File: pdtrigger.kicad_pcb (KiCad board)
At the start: 4 copper layers, 56 x 53 mm, 72 parts, among them J1 Conn_01x04_Pin, J2 USB_C_Receptacle_USB2.0_16P, Q1 DMP3098LSD-13, Q3 NMOS, SW1 SW_SPDT, U1 STM32F401RBT6, U2 CYPD3177-24LQXQ, U3 TERM_BLK, U4 SY8303AIC, Y1 16MHz

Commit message: Cleaned up schem
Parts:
- added C26: 1u, Capacitor_SMD:C_0402_1005Metric, F.Cu at (163.0, 114.5)
- added D3: YEL, LED_SMD:LED_0805_2012Metric, F.Cu at (165.2, 117.8)
- added D4: YEL, LED_SMD:LED_0805_2012Metric, F.Cu at (165.2, 120.5)
- added D5: YEL, LED_SMD:LED_0805_2012Metric, F.Cu at (165.2, 123.2)
- added D6: YEL, LED_SMD:LED_0805_2012Metric, F.Cu at (165.2, 126.0)
- added D7: YEL, LED_SMD:LED_0805_2012Metric, F.Cu at (165.2, 128.8)
- added G***: LOGO, dKiCadLib:dcLogo, F.Cu at (151.0, 137.0)
- added G***: LOGO, LOGO, F.Cu at (171.5, 112.8)
- added J3: Conn_01x02_Pin, libs:HDR-TH_2P-P2.54-V-M, F.Cu at (132.0, 97.0)
- added R27: 20k, Resistor_SMD:R_0603_1608Metric, F.Cu at (162.8, 111.9)
- added R28: 1k5, Resistor_SMD:R_0402_1005Metric, F.Cu at (163.0, 117.7)
- added R29: 1k5, Resistor_SMD:R_0402_1005Metric, F.Cu at (163.0, 120.5)
- added R30: 1k5, Resistor_SMD:R_0402_1005Metric, F.Cu at (163.0, 123.3)
- added R31: 1k5, Resistor_SMD:R_0402_1005Metric, F.Cu at (163.0, 126.0)
- added R32: 1k5, Resistor_SMD:R_0402_1005Metric, F.Cu at (163.0, 128.8)
- added SW2: SW_Push, libs:SW-SMD_L3.9-W3.0-P4.45, F.Cu at (166.5, 112.8)
- added TP1: TestPoint, TestPoint:TestPoint_THTPad_D1.5mm_Drill0.7mm, F.Cu at (180.0, 135.2)
- added TP2: TestPoint, TestPoint:TestPoint_THTPad_D1.5mm_Drill0.7mm, F.Cu at (175.0, 140.5)
- added TP3: TestPoint, TestPoint:TestPoint_THTPad_D1.5mm_Drill0.7mm, F.Cu at (134.0, 140.5)
- moved R13 0.75 mm to (143.2, 116.0)
- moved R18 0.50 mm to (151.8, 116.0)
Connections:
- net Net-(U4-LX) renamed /LX
- J2 pad S1: unconnected-(J2-SHIELD-PadS1)_2 -> GND
- U1 pad 16: unconnected-(U1-PA2-Pad16) -> /UART_TX
- U1 pad 17: unconnected-(U1-PA3-Pad17) -> /UART_RX
- U1 pad 54: unconnected-(U1-PD2-Pad54) -> /LED_PDO5
- U1 pad 55: unconnected-(U1-PB3-Pad55) -> /LED_PDO4
- U1 pad 56: unconnected-(U1-PB4-Pad56) -> /LED_PDO3
- U1 pad 57: unconnected-(U1-PB5-Pad57) -> /LED_PDO2
- U1 pad 58: unconnected-(U1-PB6-Pad58) -> /LED_PDO1
- U1 pad 59: unconnected-(U1-PB7-Pad59) -> /MODE_BTN
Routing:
- net Net-(C18-Pad2): track 10.6 -> 43.1 mm, vias 0 -> 2
- net /PD_FAULT: track 3.31 -> 31.6 mm, vias 0 -> 3
- net /LED_PDO5: track 0.00 -> 27.2 mm
- net /USB_D+: track 0.00 -> 26.9 mm, vias 0 -> 2
- net /SWDIO: track 0.00 -> 26.6 mm, vias 0 -> 1
- net /USB_D-: track 0.00 -> 26.0 mm, vias 0 -> 2
- net /LED_PDO4: track 0.00 -> 25.0 mm
- net /LED_PDO3: track 0.00 -> 22.8 mm
- net /BOOT0: track 0.00 -> 22.0 mm, vias 0 -> 2
- net /LED_PDO2: track 0.00 -> 20.7 mm
- net /SWCLK: track 0.00 -> 20.2 mm, vias 0 -> 1
- net /PD_SAFE: track 0.00 -> 18.5 mm
- net /LED_PDO1: track 0.00 -> 18.5 mm
- net /MODE_BTN: track 0.00 -> 17.4 mm
- net /UART_TX: track 0.00 -> 17.4 mm, vias 0 -> 1
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- added copper zone on In2.Cu, net +3V3_MCU
- added copper zone on F.Cu, net /LX
- added copper zone on B.Cu, net GND
- added copper zone on F.Cu, net GND
- added copper zone on In1.Cu, net GND
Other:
- board text added: "12V"
- board text added: "15V"
- board text added: "20V"
- board text added: "5V"
- board text added: "9V"
- board text added: "GND"
- board text added: "JLCJLCJLCJLC"
- board text added: "LC 3 Sep 2025"
- board text added: "PDO"
- board text added: "RX"
- board text added: "TX"
- board text added: "USB-C PD Trigger"
- board text added: "VIN"
- board text added: "VOUT"
- board text removed: "DNP"

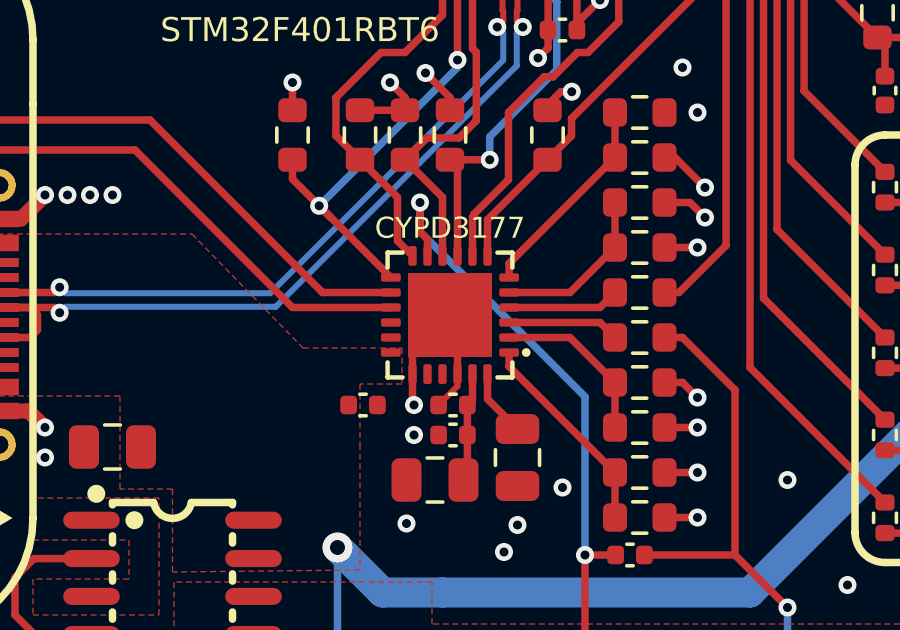
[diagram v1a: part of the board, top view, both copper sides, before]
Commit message: added GND via-in-pad to CYPD3177 IC
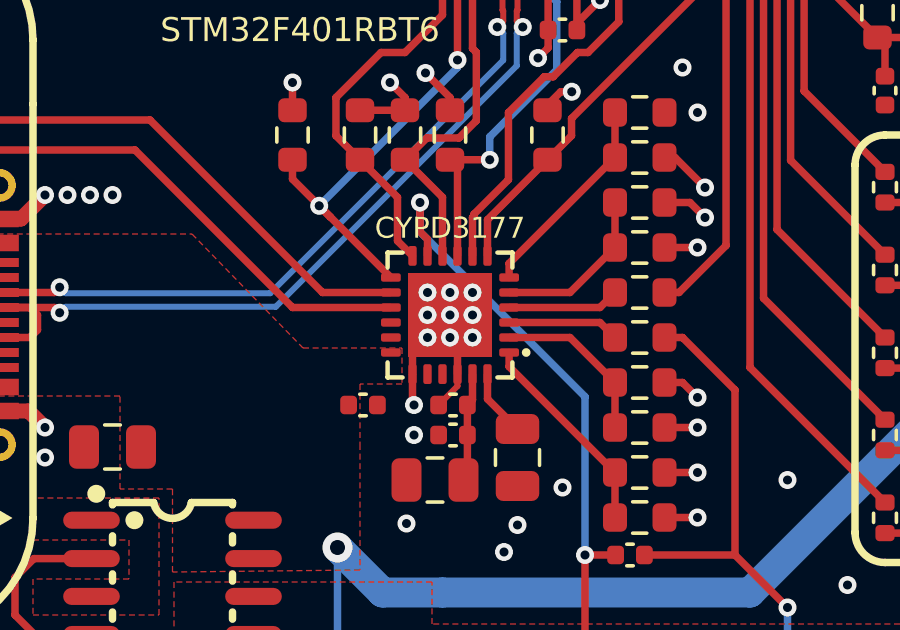
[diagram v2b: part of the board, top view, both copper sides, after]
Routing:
- net GND: vias 124 -> 133
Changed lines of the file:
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@@
 			(pinfunction "1")
 			(pintype "power_in")
-			(zone_connect 2)
 		)
 		(pad "2" thru_hole circle
@@
 			(pinfunction "2")
 			(pintype "power_in")
-			(zone_connect 2)
 		)
 		(embedded_fonts no)
 		(model "/libs.3dshapes/CONN-TH_P5.00_KF301-5.0-2P.wrl"
 			(offset
-				(xyz 0.3 0.2 4.93)
+				(xyz -0 0.2 4.92)
 			)
 			(scale
@@
 			(pinfunction "C")
 			(pintype "passive")
-			(zone_connect 2)
 		)
 		(embedded_fonts no)
 		(model "/libs.3dshapes/SW-SMD_K3-1280S-K1.wrl"
 			(offset
-				(xyz 3.38 -0 0.6)
+				(xyz 3.38 -0 1)
 			)
 			(scale
@@
 			)
 			(rotate
-				(xyz 0 0 0)
+				(xyz -0 -0 -0)
 			)
 		)
@@
 	)
 	(via
+		(at 147.75 121.25)
+		(size 0.6)
+		(drill 0.3)
+		(layers "F.Cu" "B.Cu")
+		(net 1)
+	)
+	(via
 		(at 147.05 128.95)
 		(size 0.6)
@@
 	)
 	(via
+		(at 148.5 122.75)
+		(size 0.6)
+		(drill 0.3)
+		(layers "F.Cu" "B.Cu")
+		(net 1)
+	)
+	(via
 		(at 153 94.75)
 		(size 0.6)
@@
 	)
 	(via
+		(at 149.25 121.25)
+		(size 0.6)
+		(drill 0.3)
+		(layers "F.Cu" "B.Cu")
+		(net 1)
+	)
+	(via
 		(at 149 91.5)
 		(size 0.6)
@@
 	)
 	(via
+		(at 147.75 122.75)
+		(size 0.6)
+		(drill 0.3)
+		(layers "F.Cu" "B.Cu")
+		(net 1)
+	)
+	(via
 		(at 167.5 127.5)
 		(size 0.6)
@@
 	)
 	(via
+		(at 147.75 122)
+		(size 0.6)
+		(drill 0.3)
+		(layers "F.Cu" "B.Cu")
+		(net 1)
+	)
+	(via
 		(at 145.5 95.5)
 		(size 0.6)
@@
 	)
 	(via
+		(at 149.25 122.75)
+		(size 0.6)
+		(drill 0.3)
+		(layers "F.Cu" "B.Cu")
+		(net 1)
+	)
+	(via
 		(at 148.5 103)
 		(size 0.6)
@@
 	)
 	(via
+		(at 149.25 122)
+		(size 0.6)
+		(drill 0.3)
+		(layers "F.Cu" "B.Cu")
+		(net 1)
+	)
+	(via
 		(at 181.25 118.25)
 		(size 0.6)
@@
 	)
 	(via
+		(at 148.5 121.25)
+		(size 0.6)
+		(drill 0.3)
+		(layers "F.Cu" "B.Cu")
+		(net 1)
+	)
+	(via
 		(at 150.3 129.9)
 		(size 0.6)
 		(drill 0.3)
+		(layers "F.Cu" "B.Cu")
+		(net 1)
+	)
+	(via
+		(at 148.5 122)
+		(size 0.6)
+		(drill 0.3)

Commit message: Changed as per design review
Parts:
- added D8: USBLC6-2P6, libs:SOT-666-6_L1.6-W1.2-P0.50-LS1.6-BR, F.Cu at (136.5, 121.5)
- added D9: USBLC6-2P6, libs:SOT-666-6_L1.6-W1.2-P0.50-LS1.6-BR, F.Cu at (136.3, 116.0)
- renumbered TP2 to TP3, TP1 to TP3
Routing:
- net /VBUS: track 68.1 -> 72.9 mm, vias 4 -> 6
- net GND: track 36.2 -> 38.6 mm, vias 133 -> 135
